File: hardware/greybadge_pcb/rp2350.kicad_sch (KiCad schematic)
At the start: 39 parts, among them J5 USB_C_Receptacle_USB2.0, U4 W25Q128JVS, U5 RP2350_60QFN, U6 NCP1117-3.3_SOT223, Y1 12Mhz

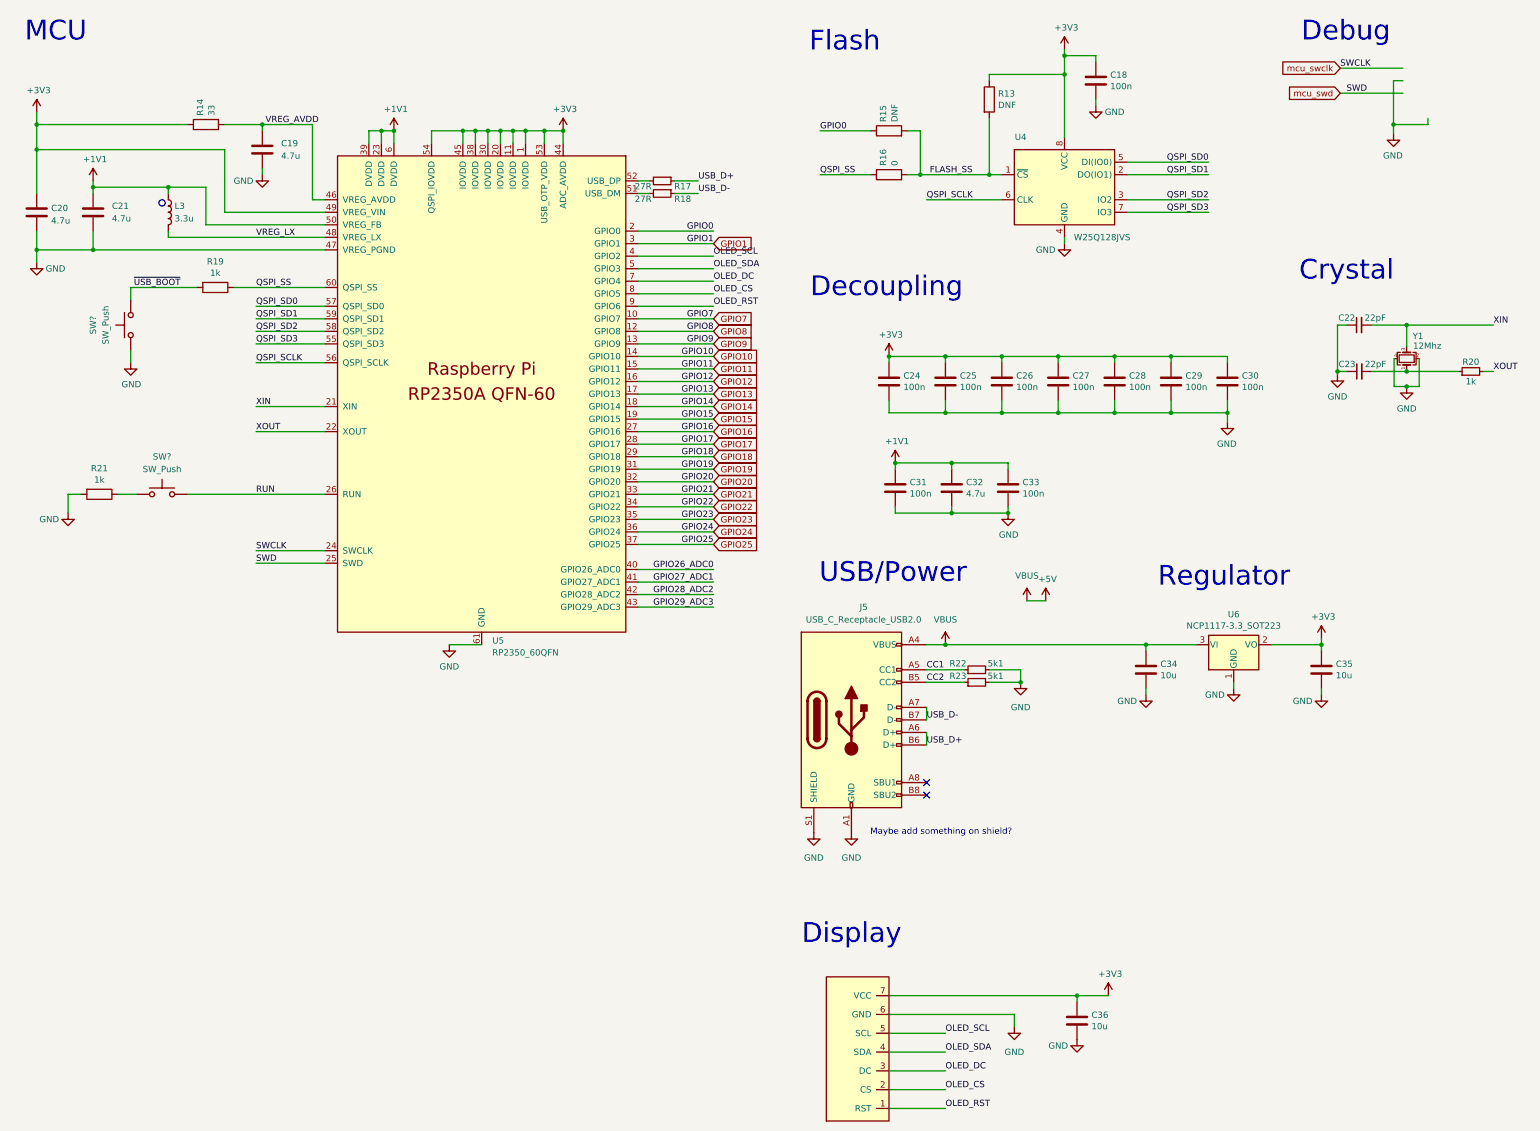
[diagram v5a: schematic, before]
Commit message: feat: routing cleanupish, power splitting and drc
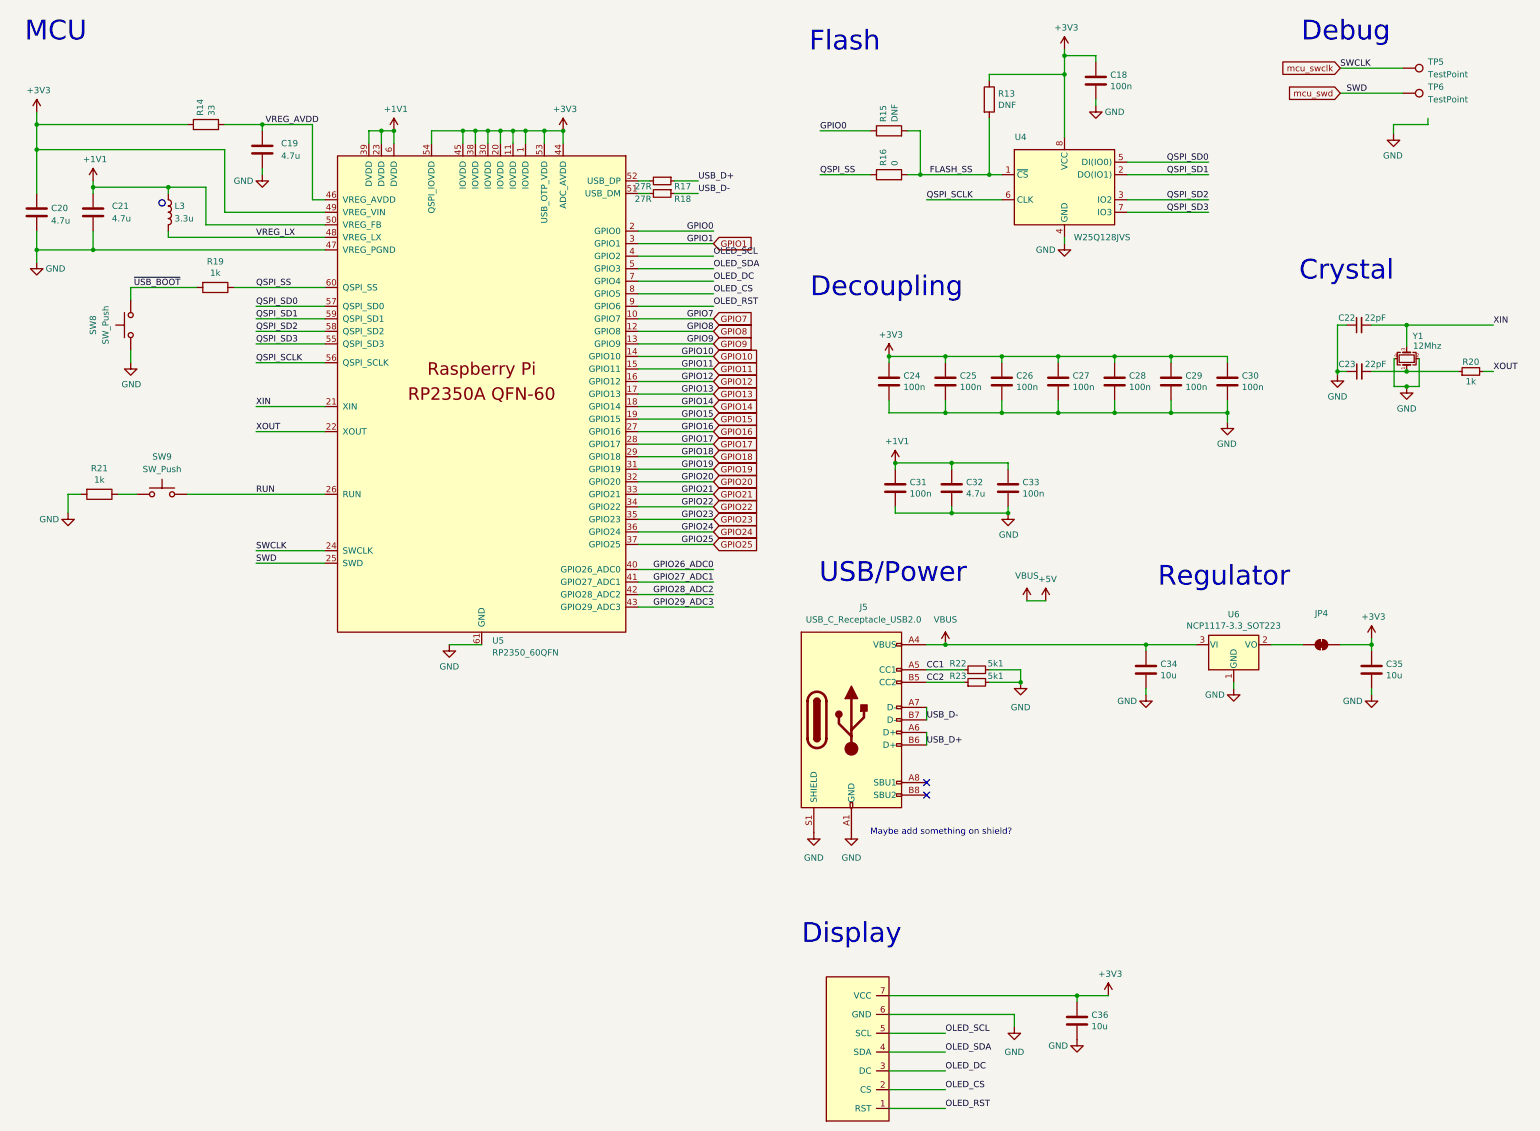
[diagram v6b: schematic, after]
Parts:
- added JP4: SolderJumper_2_Bridged, Jumper:SolderJumper-2_P1.3mm_Bridged2Bar_RoundedPad1.0x1.5mm, symbol Jumper:SolderJumper_2_Bridged
- added TP5, TP6: TestPoint, TestPoint:TestPoint_Pad_D1.5mm, symbol Connector:TestPoint
- GC9A1: footprint footprints:GC9A01 -> custom:GC9A01
- gave numbers to parts that had none: 2
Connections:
- net +3V3: now also JP4.2 (B); no longer U6.2 (VO)
- net mcu_swclk: now also TP5.1
- net mcu_swd: now also TP6.1
- new net: JP4.1 (A), U6.2 (VO)
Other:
- moved on the sheet: C35

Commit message: Clean up PCB
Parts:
- C33: renamed from C34; footprint Capacitor_SMD:C_0805_2012Metric -> Capacitor_SMD:C_0402_1005Metric
- C34: renamed from C35; footprint Capacitor_SMD:C_0805_2012Metric -> Capacitor_SMD:C_0402_1005Metric
- C35: renamed from C36; footprint Capacitor_SMD:C_0805_2012Metric -> Capacitor_SMD:C_0402_1005Metric
- renumbered C18 to C17, C19 to C18, C20 to C19, C21 to C20, C22 to C21, C23 to C22, C24 to C23, C25 to C24, C26 to C25, C27 to C26, C28 to C27, C29 to C28, C30 to C29, C31 to C30, C32 to C31, C33 to C32, R13 to R21, R14 to R22, R15 to R23, R16 to R24, R17 to R25, R18 to R26, R19 to R27, R20 to R28, R21 to R29, R22 to R30, R23 to R31, TP5 to TP4, TP6 to TP5

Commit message: Update PCB and add JLC files
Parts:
- removed R21: DNF, Resistor_SMD:R_0402_1005Metric, symbol Device:R
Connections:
- net FLASH_SS is gone; now on net +3V3: R23.2, R24.2, U4.1 (~{CS})
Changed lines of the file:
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@@
 	(wire
 		(pts
-			(xy 218.44 39.37) (xy 218.44 50.8)
-		)
-		(stroke
-			(width 0)
-			(type default)
-		)
-	)
-	(wire
-		(pts
 			(xy 119.38 44.45) (xy 119.38 41.91)
 		)
@@
 	(wire
 		(pts
-			(xy 218.44 31.75) (xy 218.44 30.48)
+			(xy 218.44 30.48) (xy 218.44 50.8)
 		)
 		(stroke
@@
 					(unit 1)
 				)
-			)
-		)
-	)
-	(symbol
-		(lib_id "Device:R")
-		(at 218.44 35.56 0)
-		(unit 1)
-		(exclude_from_sim no)
-		(in_bom yes)
-		(on_board yes)
-		(dnp no)
-		(property "Reference" "R21"
-			(at 220.218 34.3916 0)
-			(effects
-				(font
-					(size 1.27 1.27)
-				)
-				(justify left)
-			)
-		)
-		(property "Value" "DNF"
-			(at 220.218 36.703 0)
-			(effects
-				(font
-					(size 1.27 1.27)
-				)
-				(justify left)
-			)
-		)
-		(property "Footprint" "Resistor_SMD:R_0402_1005Metric"
-			(at 216.662 35.56 90)
-			(effects
-				(font
-					(size 1.27 1.27)
-				)
-				(hide yes)
-			)
-		)
-		(property "Datasheet" "~"
-			(at 218.44 35.56 0)
-			(effects
-				(font
-					(size 1.27 1.27)
-				)
-				(hide yes)
-			)
-		)
-		(property "Description" ""
-			(at 218.44 35.56 0)
-			(effects
-				(font
-					(size 1.27 1.27)
-				)
-			)
-		)
-		(pin "1"
-		)
-		(pin "2"
-		)
-		(instances
-			(project "greybadge_pcb"
-				(path "/4eb7ff30-5b75-4e83-8e37-4e6cd7a9e830/9563b0f2-de2f-44b6-a21c-14dec17cccec"
-					(reference "R21")
-					(unit 1)
-				)
